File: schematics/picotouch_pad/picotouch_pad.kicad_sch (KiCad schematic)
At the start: 98 parts, among them J1 AudioJack4, SW1 SSSS811101, U1 Pico, U2 MCP73831-2-OT, X1 AFC20-S02ACA-00

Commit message: new silkscreen and fixes
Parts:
- added PAD24: 1, todbot_stuff:Pad-CapTouch-10x5mm-roundrect, symbol todbot_stuff:Capacitive_Button
- added R28: 1M, Resistor_SMD:R_0603_1608Metric, symbol Device:R
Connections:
- net GND: now also R28.2
- net TOUCH24: now reaches U1.31 (GPIO26_ADC0)
- net TOUCH24: now also PAD24.1 (A), R28.1
- no-connect marks 12 -> 10
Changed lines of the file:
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@@
 	)
 	(junction
+		(at 389.89 219.71)
+		(diameter 0)
+		(color 0 0 0 0)
+	)
+	(junction
 		(at 327.66 187.96)
 		(diameter 0)
@@
 	)
 	(no_connect
-		(at 91.44 53.34)
-	)
-	(no_connect
 		(at 78.74 40.64)
 	)
@@
 	)
 	(no_connect
-		(at 91.44 55.88)
-	)
-	(no_connect
 		(at 36.83 139.7)
 	)
@@
 	(wire
 		(pts
+			(xy 386.08 219.71) (xy 389.89 219.71)
+		)
+		(stroke
+			(width 0)
+			(type default)
+		)
+	)
+	(wire
+		(pts
 			(xy 248.92 187.96) (xy 252.73 187.96)
 		)
@@
 	(wire
 		(pts
+			(xy 386.08 210.82) (xy 386.08 219.71)
+		)
+		(stroke
+			(width 0)
+			(type default)
+		)
+	)
+	(wire
+		(pts
 			(xy 311.15 187.96) (xy 314.96 187.96)
 		)
@@
 		)
 	)
+	(label "TOUCH24"
+		(at 82.55 55.88 0)
+		(fields_autoplaced yes)
+		(effects
+			(font
+				(size 1.27 1.27)
+			)
+			(justify left bottom)
+		)
+	)
 	(label "TOUCH4"
 		(at 226.06 180.34 0)
@@
 		)
 	)
+	(label "TOUCH24"
+		(at 386.08 210.82 0)
+		(fields_autoplaced yes)
+		(effects
+			(font
+				(size 1.27 1.27)
+			)
+			(justify left bottom)
+		)
+	)
 	(label "TOUCH10"
 		(at 298.45 179.07 0)
@@
 	(symbol
 		(lib_id "power:GND")
+		(at 389.89 227.33 0)
+		(unit 1)
+		(exclude_from_sim no)
+		(in_bom yes)
+		(on_board yes)
+		(dnp no)
+		(fields_autoplaced yes)
+		(property "Reference" "#PWR0123"
+			(at 389.89 233.68 0)
+			(effects
+				(font
+					(size 1.27 1.27)
+				)
+				(hide yes)
+			)
+		)
+		(property "Value" "GND"
+			(at 389.89 232.41 0)
+			(effects
+				(font
+					(size 1.27 1.27)
+				)
+			)
+		)
+		(property "Footprint" ""
+			(at 389.89 227.33 0)
+			(effects
+				(font
+					(size 1.27 1.27)
+				)
+				(hide yes)
+			)
+		)
+		(property "Datasheet" ""
+			(at 389.89 227.33 0)
+			(effects
+				(font
+					(size 1.27 1.27)
+				)
+				(hide yes)
+			)
+		)
+		(property "Description" "Power symbol creates a global label with name \"GND\" , ground"
+			(at 389.89 227.33 0)
+			(effects
+				(font
+					(size 1.27 1.27)
+				)
+				(hide yes)
+			)
+		)
+		(pin "1"
+		)
+		(instances
+			(project "picotouch_pad"
+				(path "/a83b8b47-e572-48e2-b6f7-0ec1c4c903c4"
+					(reference "#PWR0123")
+					(unit 1)
+				)
+			)
+		)
+	)
+	(symbol
+		(lib_id "power:GND")
 		(at 262.89 92.71 0)
 		(unit 1)
@@
 	(symbol
 		(lib_id "todbot_stuff:Capacitive_Button")
+		(at 389.89 219.71 0)
+		(unit 1)
+		(exclude_from_sim no)
+		(in_bom yes)
+		(on_board yes)
+		(dnp no)
+		(property "Reference" "PAD24"
+			(at 392.43 214.6299 0)
+			(effects
+				(font
+					(size 1.27 1.27)
+				)
+				(justify left)
+			)
+		)
+		(property "Value" "1"
+			(at 392.43 217.1699 0)
+			(effects
+				(font
+					(size 1.27 1.27)
+				)
+				(justify left)
+			)
+		)
+		(property "Footprint" "todbot_stuff:Pad-CapTouch-10x5mm-roundrect"
+			(at 389.89 227.33 0)
+			(effects
+				(font
+					(size 1.27 1.27)
+				)
+				(hide yes)
+			)
+		)
+		(property "Datasheet" "~"
+			(at 389.89 229.87 0)
+			(effects
+				(font
+					(size 1.27 1.27)
+				)
+				(hide yes)
+			)
+		)
+		(property "Description" "Capacitive touch pad"
+			(at 389.89 219.71 0)
+			(effects
+				(font
+					(size 1.27 1.27)
+				)
+				(hide yes)
+			)
+		)
+		(pin "1"
+		)
+		(instances
+			(project "picotouch_pad"
+				(path "/a83b8b47-e572-48e2-b6f7-0ec1c4c903c4"
+					(reference "PAD24")
+					(unit 1)
+				)
+			)
+		)
+	)
+	(symbol
+		(lib_id "todbot_stuff:Capacitive_Button")
 		(at 353.06 187.96 0)
 		(unit 1)
@@
 					(unit 1)
 				)
+			)
+		)
+	)
+	(symbol
+		(lib_id "Device:R")
+		(at 389.89 223.52 0)
+		(unit 1)
+		(exclude_from_sim no)
+		(in_bom yes)
+		(on_board yes)
+		(dnp no)
+		(fields_autoplaced yes)
+		(property "Reference" "R28"
+			(at 392.43 222.2499 0)
+			(effects
+				(font
+					(size 1.27 1.27)
+				)
+				(justify left)
+			)
+		)
+		(property "Value" "1M"
+			(at 392.43 224.7899 0)
+			(effects
+				(font
+					(size 1.27 1.27)
+				)
+				(justify left)
+			)
+		)
+		(property "Footprint" "Resistor_SMD:R_0603_1608Metric"
+			(at 388.112 223.52 90)
+			(effects
+				(font
+					(size 1.27 1.27)
+				)
+				(hide yes)
+			)
+		)
+		(property "Datasheet" "~"
+			(at 389.89 223.52 0)
+			(effects
+				(font
+					(size 1.27 1.27)
+				)
+				(hide yes)
+			)
+		)
+		(property "Description" "Resistor"
+			(at 389.89 223.52 0)
+			(effects
+				(font
+					(size 1.27 1.27)
+				)
+				(hide yes)
+			)
+		)
+		(pin "1"
+		)
+		(pin "2"
+		)
+		(instances
+			(project "picotouch_pad"
+				(path "/a83b8b47-e572-48e2-b6f7-0ec1c4c903c4"
+					(reference "R28")
+					(unit 1)
+				)

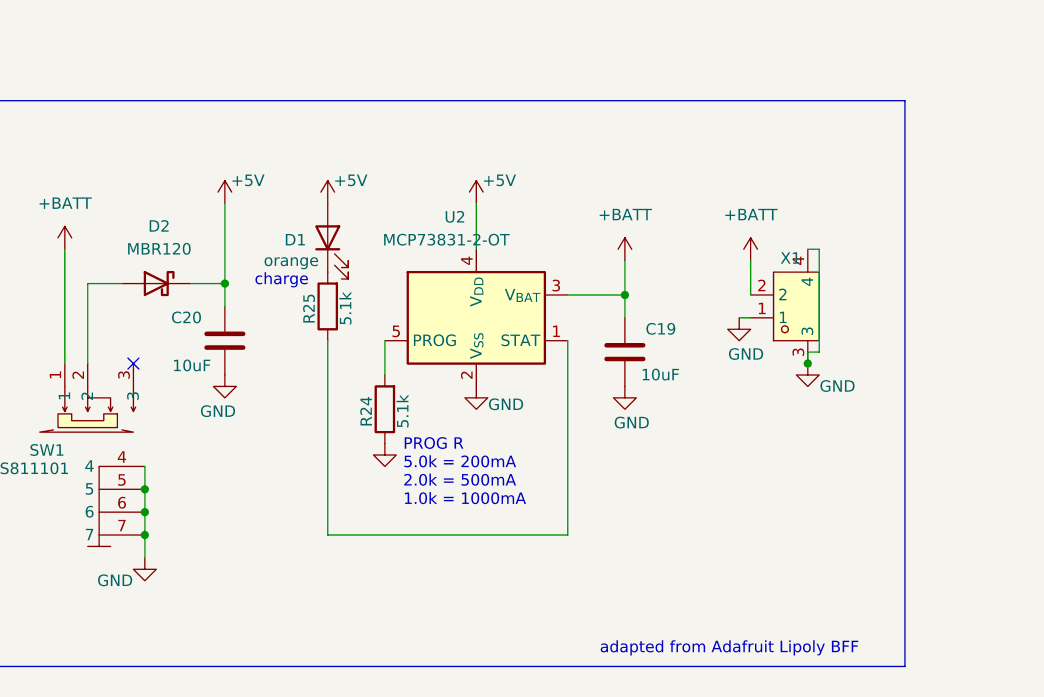
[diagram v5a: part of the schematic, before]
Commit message: resize, cleanup, change battery charge chip sch symbol
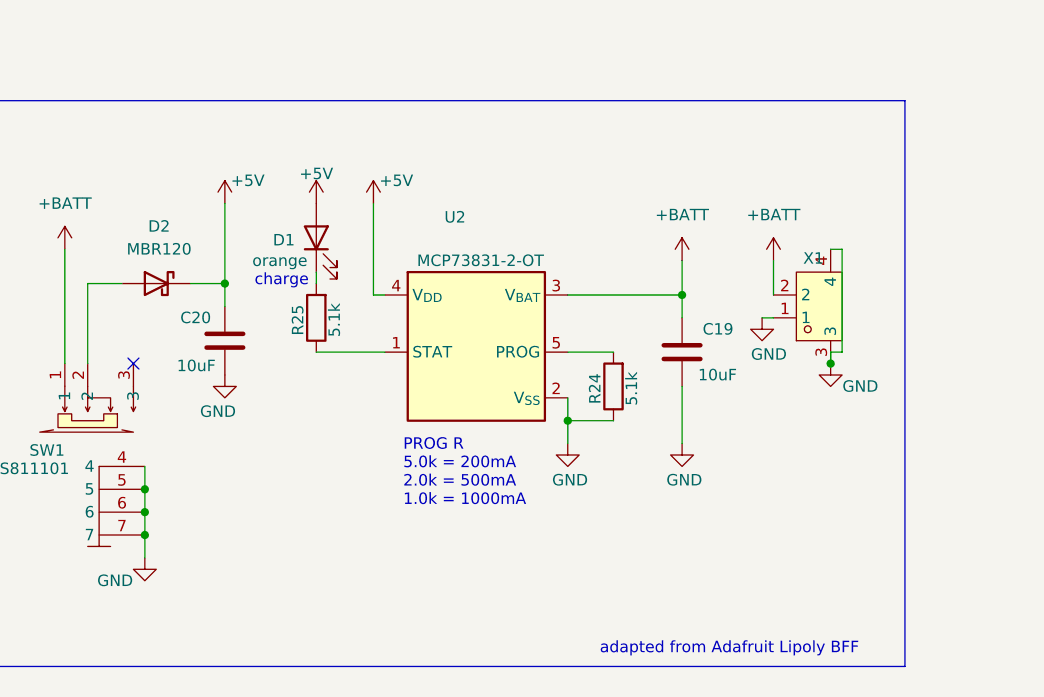
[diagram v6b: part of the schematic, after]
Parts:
- U2: symbol Battery_Management:MCP73831-2-OT -> todbot_stuff:MCP73831-2-OT
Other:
- moved on the sheet: C19, D1, R24, R25, U2, X1

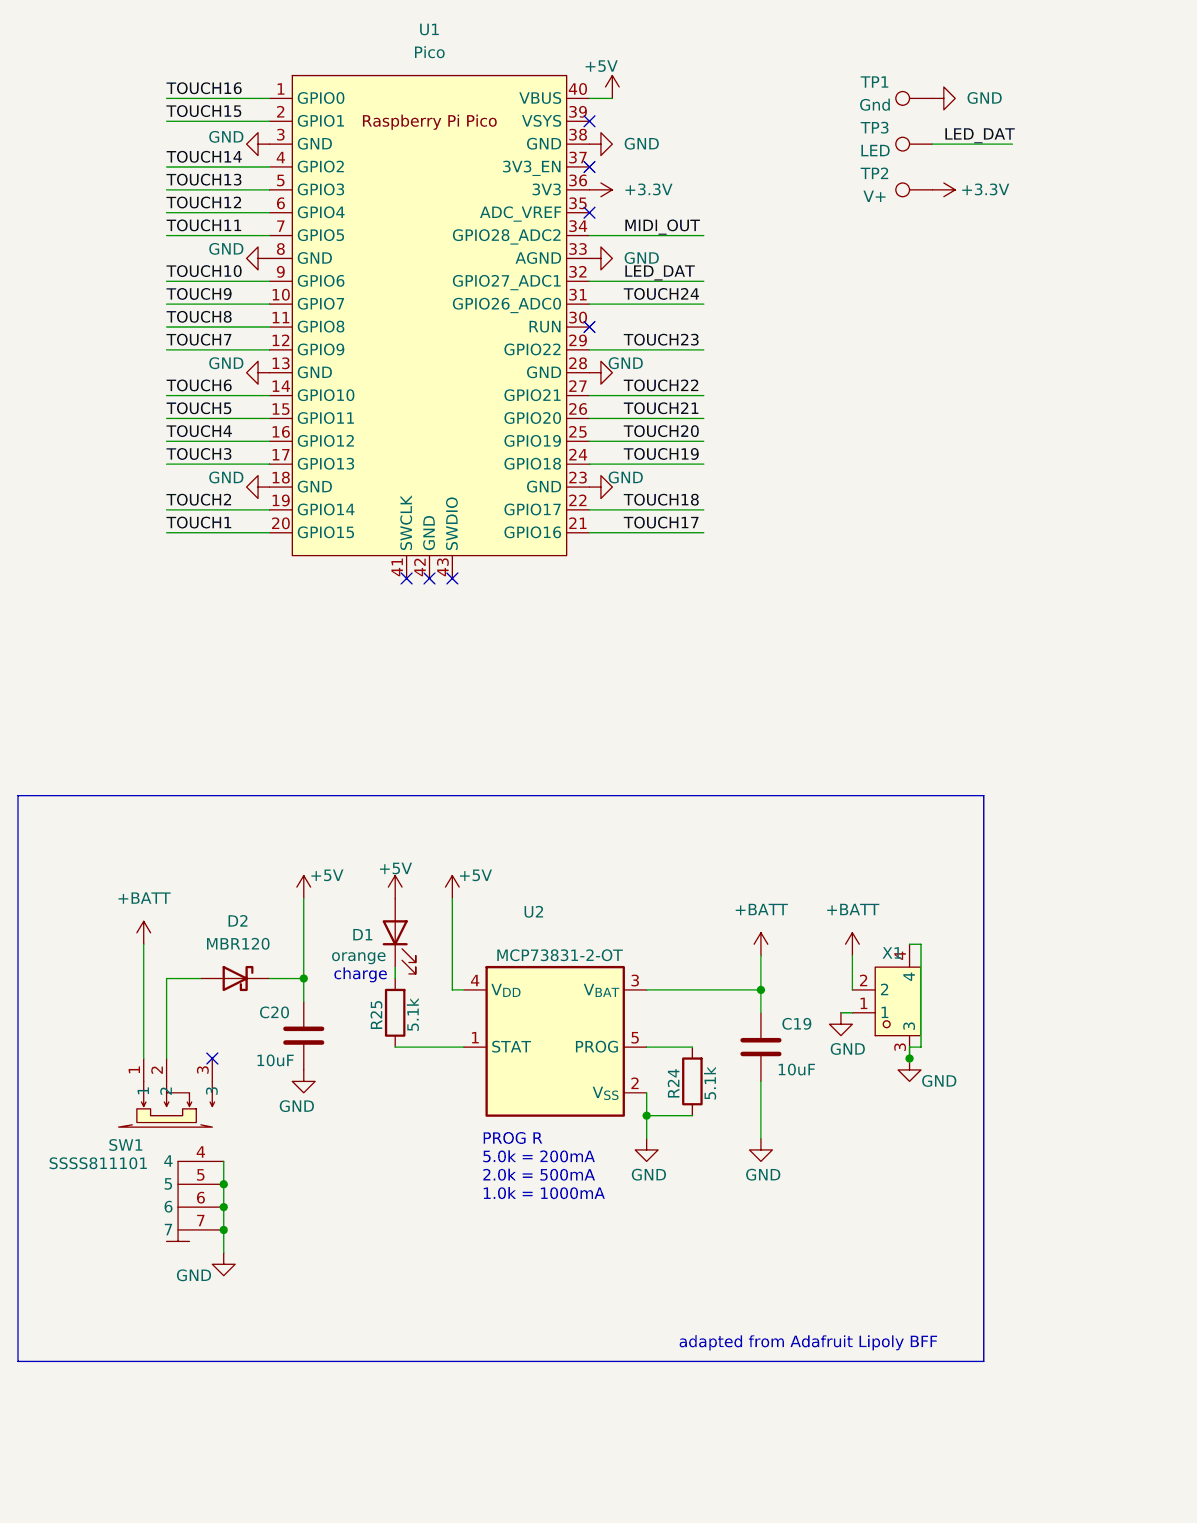
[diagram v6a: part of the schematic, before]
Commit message: add vbus diode, fix up power layout a bit
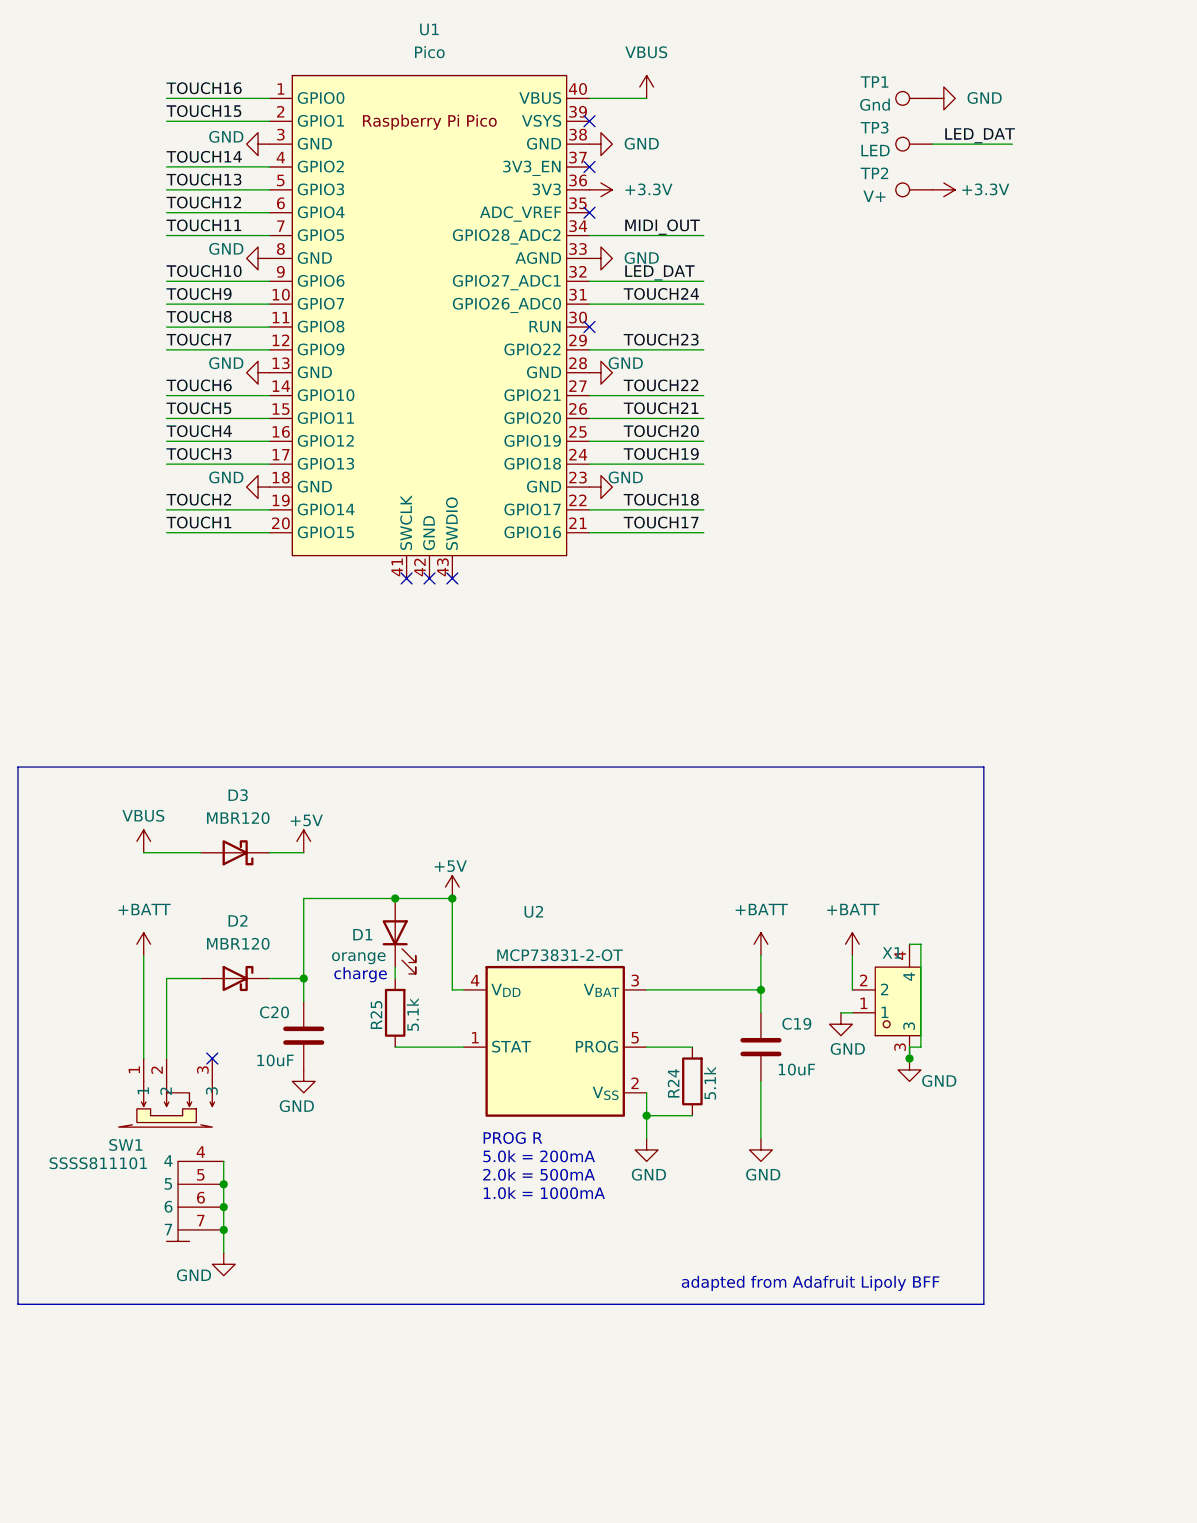
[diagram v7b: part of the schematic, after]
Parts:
- added D3: MBR120, Diode_SMD:D_SOD-123F, symbol Device:D_Schottky
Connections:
- net +5V: now also D3.1 (K); no longer U1.40 (VBUS)
- new net VBUS: D3.2 (A), U1.40 (VBUS)

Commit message: cleanup and new silkscreen
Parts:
- added C18: 100n, Capacitor_SMD:C_0603_1608Metric, symbol Device:C
- added H1, H2: MountingHole, MountingHole:MountingHole_2.7mm_M2.5, symbol Mechanical:MountingHole
- added LED18: SK6812SIDE, todbot_stuff:LED-SMD_4P-L4.0-W1.6-L-keepoutrev, symbol todbot_stuff:SK6812SIDE
- renumbered C18 to C19, C19 to C20, C20 to C21, LED18 to LED19
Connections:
- net +3.3V: now also C18.1, LED18.2 (VDD)
- net GND: now also C18.2, LED18.4 (GND)
- net at LED17.3 (DOUT): now also LED18.1 (DIN); no longer LED19.1 (DIN)
- new net: LED18.3 (DOUT), LED19.1 (DIN)
- no-connect marks 10 -> 9
